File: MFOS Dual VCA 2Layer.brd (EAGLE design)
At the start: 98.7 x 57.1 mm, 61 parts, among them IC1 TL072P, IC2 LM13700N, Q1 2N3904, Q2 2N3904, Q3 2N3906, Q4 2N3906, U1 POWER

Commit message: switched back to custom flexitrimmers
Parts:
- BIAS1, BIAS2, TRIM1, TRIM2: device pot:S64YW -> pot:B64W
- moved TRIM2 12.7 mm to (38.1, 53.3), turned to 0 degrees
- moved BIAS2 12.6 mm to (47.0, 44.5), turned to 90 degrees
- moved TRIM1 2.84 mm to (47.0, 24.1)
- moved BIAS1 1.27 mm to (52.1, 24.1)
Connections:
- net N$18: now also BIAS1.P$1
- net N$23: now also TRIM1.P$1
- net N$28: now also BIAS2.P$1
- net N$30: now also TRIM2.P$1
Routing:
- net -12V: track 190.9 -> 242.9 mm
- net N$17: track 48.1 -> 92.3 mm, vias 1 -> 0
- net N$8: track 56.8 -> 91.4 mm
- net +12V: track 208.2 -> 232.6 mm
- net N$16: track 36.9 -> 55.8 mm, vias 0 -> 1
- net GND: track 282.0 -> 300.4 mm
- net N$9: track 83.0 -> 64.8 mm
- net N$30: track 11.5 -> 29.1 mm, vias 0 -> 1
- net N$1: track 90.7 -> 106.8 mm
- net N$28: track 23.5 -> 11.7 mm
- net N$25: track 126.2 -> 114.7 mm
- net N$11: track 35.8 -> 47.2 mm
- net N$23: track 40.6 -> 51.5 mm, vias 1 -> 0
- net N$3: track 42.3 -> 49.7 mm, vias 0 -> 1
- net N$15: track 41.6 -> 48.7 mm
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
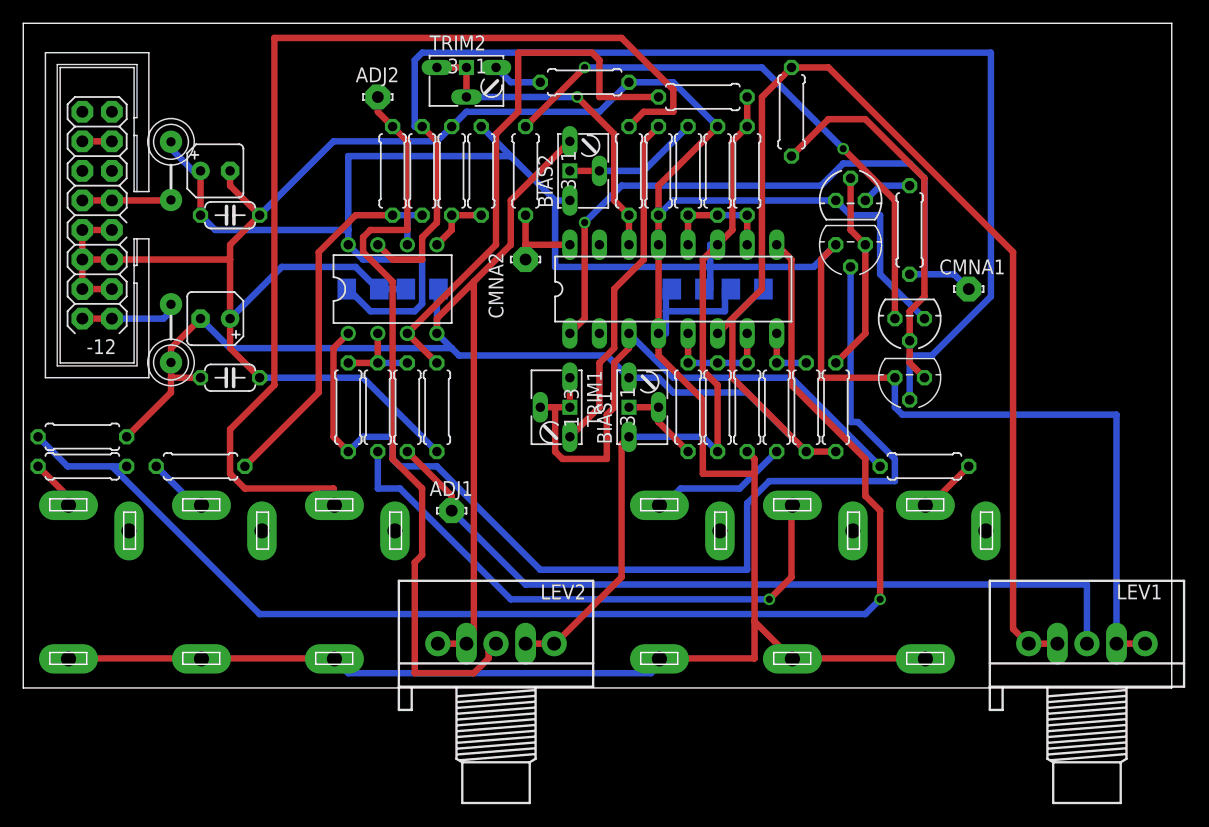
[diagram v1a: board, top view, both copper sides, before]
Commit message: symetric route sending to itead
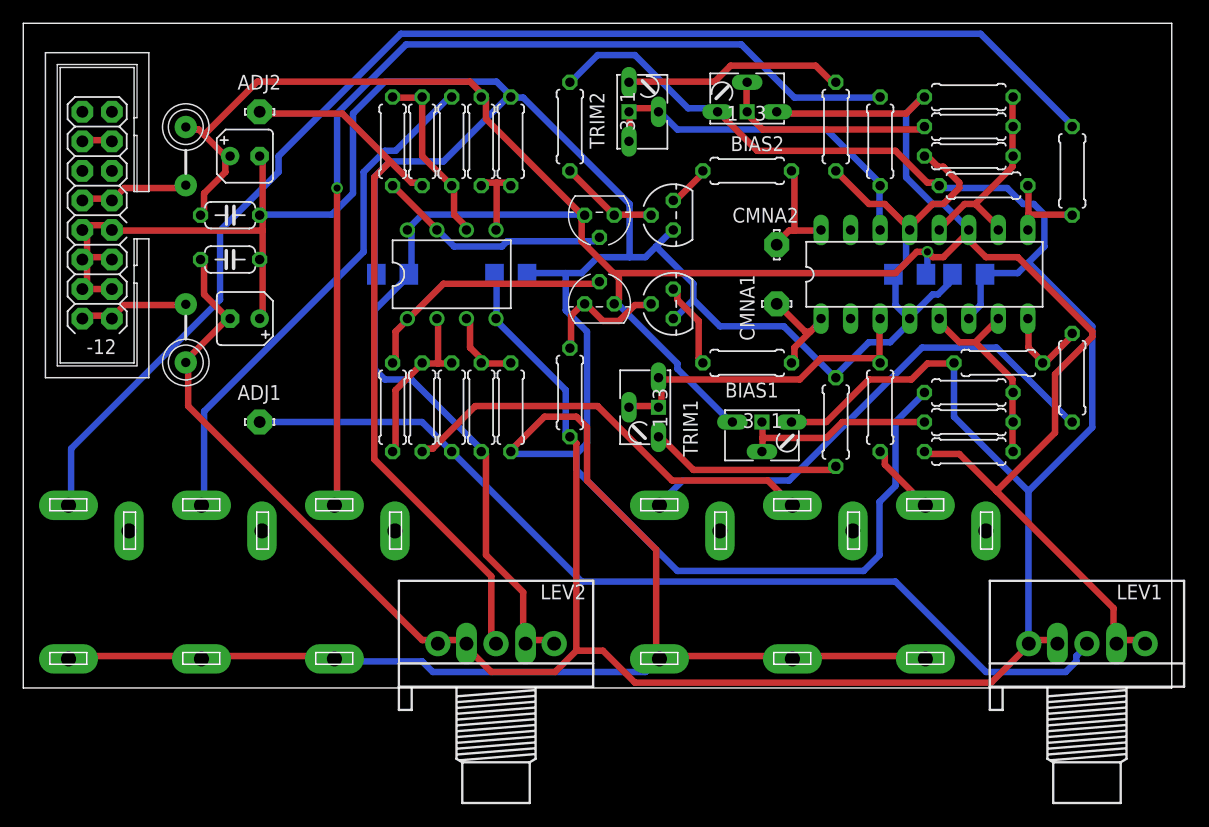
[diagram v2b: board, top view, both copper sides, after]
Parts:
- BIAS1, BIAS2: value (none) -> 100k
- TRIM1, TRIM2: value (none) -> 2k
- moved R23 88.8 mm to (90.2, 44.5), turned to 270 degrees
- moved R24 80.4 mm to (82.5, 43.2), turned to 180 degrees
- moved R7 35.3 mm to (36.8, 47.0), turned to 90 degrees
- moved R2 32.8 mm to (39.4, 24.1), turned to 90 degrees
- moved Q1 30.1 mm to (49.5, 40.6)
- moved R20 26.4 mm to (69.8, 22.9), turned to 90 degrees
- moved R14 25.5 mm to (90.2, 26.7)
- moved R27 24.4 mm to (81.3, 48.3), turned to 0 degrees
- moved R19 24.2 mm to (81.3, 22.9), turned to 0 degrees
- moved R5 22.9 mm to (47.0, 25.4)
- moved Q2 22.2 mm to (49.5, 33.0), turned to 0 degrees
- moved Q4 22.2 mm to (55.9, 40.6), turned to 90 degrees
- moved R16 21.9 mm to (81.3, 20.3), turned to 0 degrees
- moved R28 21.9 mm to (69.8, 48.3), turned to 270 degrees
- moved R22 21.7 mm to (73.7, 47.0)
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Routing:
- net N$26: track 4.42 -> 113.4 mm
- net N$25: track 114.7 -> 7.59 mm, vias 1 -> 0
- net N$1: track 106.8 -> 20.3 mm
- net N$8: track 91.4 -> 22.1 mm
- net GND: track 300.4 -> 369.1 mm
- net N$16: track 55.8 -> 8.70 mm, vias 1 -> 0
- net N$15: track 48.7 -> 3.76 mm, vias 2 -> 0
- net N$11: track 47.2 -> 6.90 mm
- net N$4: track 5.32 -> 44.6 mm
- net N$19: track 11.9 -> 43.8 mm
- net +12V: track 232.6 -> 260.5 mm, vias 0 -> 1
- net N$14: track 33.0 -> 8.60 mm
- net -12V: track 242.9 -> 267.0 mm
- net N$23: track 51.5 -> 28.8 mm
- net N$10: track 33.8 -> 15.5 mm
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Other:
- board text added: "Release v0.1"
- board text added: "https://github.com/jbeuckm/MFOS-Dual-VCA-2Layer.git"
